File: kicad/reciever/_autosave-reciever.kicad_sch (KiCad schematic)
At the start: 12 parts, among them U2 LM2596T-5

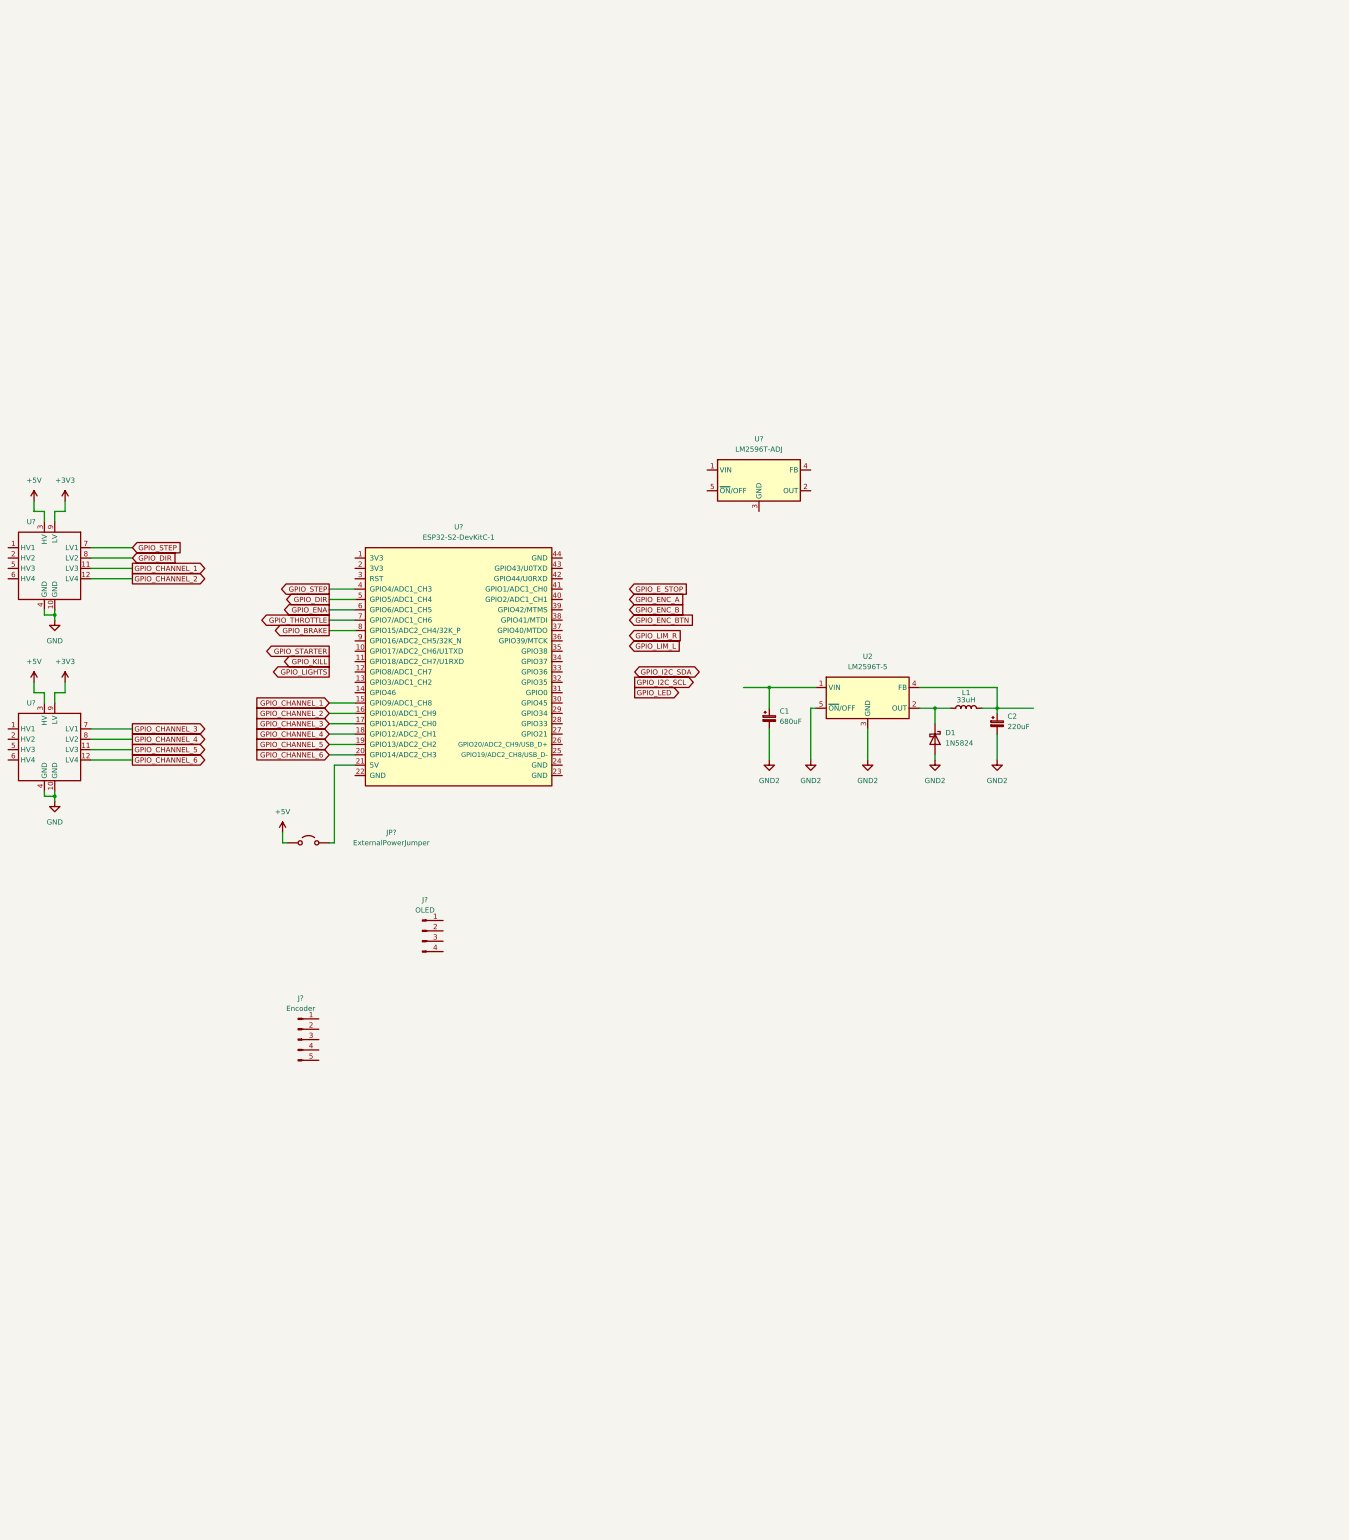
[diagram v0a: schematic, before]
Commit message: throttle servo behaves as expected, brake servo goes all the way and does not come back
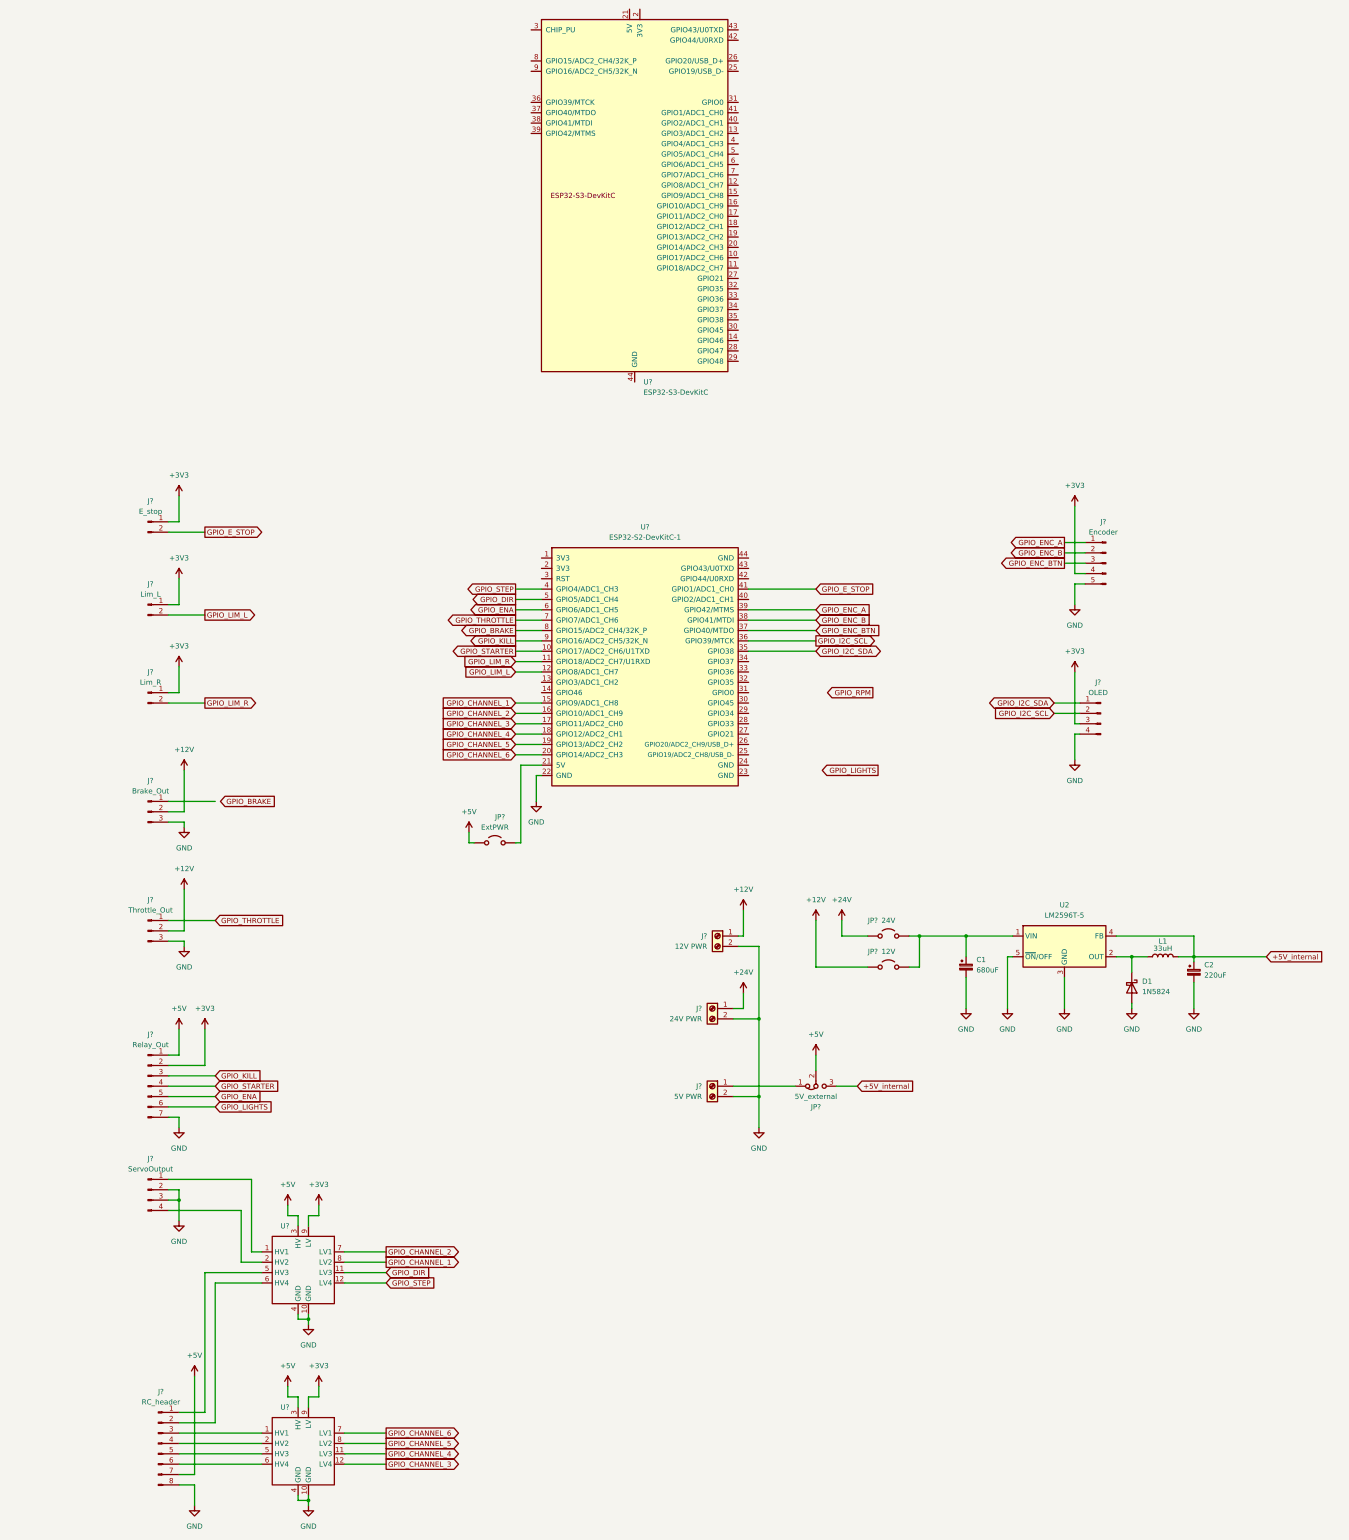
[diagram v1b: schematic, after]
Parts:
- removed U?: LM2596T-ADJ, Package_TO_SOT_THT:TO-220-5_P3.4x3.7mm_StaggerOdd_Lead3.8mm_Vertical, symbol Regulator_Switching:LM2596T-ADJ
- added J?: ServoOutput, symbol Connector:Conn_01x04_Pin
- added J?: 12V PWR, symbol Connector:Screw_Terminal_01x02
- added J?: Throttle_Out, symbol Connector:Conn_01x03_Pin
- added J?: Lim_L, symbol Connector:Conn_01x02_Pin
- added J?: 5V PWR, symbol Connector:Screw_Terminal_01x02
- added J?: Lim_R, symbol Connector:Conn_01x02_Pin
- added J?: Relay_Out, symbol Connector:Conn_01x07_Pin
- added J?: RC_header, symbol Connector:Conn_01x08_Pin
- added J?: Brake_Out, symbol Connector:Conn_01x03_Pin
- added J?: 24V PWR, symbol Connector:Screw_Terminal_01x02
- added J?: E_stop, symbol Connector:Conn_01x02_Pin
- added JP?: 5V_external, symbol Jumper:Jumper_3_Bridged12
- added JP?: 24V, symbol Jumper:Jumper_2_Open
- added JP?: 12V, symbol Jumper:Jumper_2_Open
- added U?: ESP32-S3-DevKitC, PCM_Espressif:ESP32-S3-DevKitC, symbol Espressif:ESP32-S3-DevKitC
- JP?: value ExternalPowerJumper -> ExtPWR
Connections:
- net GND2 is gone; now on net GND: C1.2, C2.2, D1.2 (A), U2.3 (GND), U2.5 (~{ON}/OFF)
- net +3V3: now also J?.3 (Pin_3), J?.4 (Pin_4), J?.1 (Pin_1), J?.1 (Pin_1), J?.1 (Pin_1), J?.2 (Pin_2)
- net +5V: now also J?.1 (Pin_1), J?.7 (Pin_7), JP?.2 (C)
- net GND: now also J?.4 (Pin_4), J?.5 (Pin_5), U?.22 (GND), J?.2 (Pin_2), J?.2 (Pin_2), J?.2 (Pin_2), J?.2 (Pin_2), J?.3 (Pin_3), J?.3 (Pin_3), J?.3 (Pin_3), J?.7 (Pin_7), J?.8 (Pin_8)
- net GPIO_CHANNEL_1: now also U?.8 (LV2); no longer U?.11 (LV3)
- net GPIO_CHANNEL_2: now also U?.7 (LV1); no longer U?.12 (LV4)
- net GPIO_CHANNEL_3: now also U?.12 (LV4); no longer U?.7 (LV1)
- net GPIO_CHANNEL_4: now also U?.11 (LV3); no longer U?.8 (LV2)
- net GPIO_CHANNEL_5: now also U?.8 (LV2); no longer U?.11 (LV3)
- net GPIO_CHANNEL_6: now also U?.7 (LV1); no longer U?.12 (LV4)
- net GPIO_DIR: now also U?.11 (LV3); no longer U?.8 (LV2)
- net GPIO_ENA: now also J?.5 (Pin_5)
- net GPIO_ENC_A: now also J?.1 (Pin_1), U?.39 (GPIO42/MTMS)
- net GPIO_ENC_B: now also J?.2 (Pin_2), U?.38 (GPIO41/MTDI)
- net GPIO_ENC_BTN: now also J?.3 (Pin_3), U?.37 (GPIO40/MTDO)
- net GPIO_E_STOP: now also U?.41 (GPIO1/ADC1_CH0), J?.2 (Pin_2)
- net GPIO_I2C_SCL: now also J?.2 (Pin_2), U?.36 (GPIO39/MTCK)
- net GPIO_I2C_SDA: now also J?.1 (Pin_1), U?.35 (GPIO38)
- net GPIO_KILL: now also U?.9 (GPIO16/ADC2_CH5/32K_N), J?.3 (Pin_3)
- net GPIO_LIGHTS: now also J?.6 (Pin_6)
- net GPIO_LIM_L: now also U?.12 (GPIO8/ADC1_CH7), J?.2 (Pin_2)
- net GPIO_LIM_R: now also U?.11 (GPIO18/ADC2_CH7/U1RXD), J?.2 (Pin_2)
- net GPIO_STARTER: now also U?.10 (GPIO17/ADC2_CH6/U1TXD), J?.4 (Pin_4)
- net GPIO_STEP: now also U?.12 (LV4); no longer U?.7 (LV1)
- net GPIO_THROTTLE: now also J?.1 (Pin_1)
- net at C1.1, U2.1 (VIN): now also JP?.2 (B), JP?.2 (B)
- net +5V_internal: now reaches C2.1, L1.2, U2.4 (FB)
- net +5V_internal: now also JP?.3 (B)
- net at U?.1 (HV1): now also J?.1 (Pin_1)
- net at U?.2 (HV2): now also J?.4 (Pin_4) (x2)
- net at U?.5 (HV3): now also J?.1 (Pin_1)
- net at U?.6 (HV4): now also J?.2 (Pin_2)
- net at U?.1 (HV1): now also J?.3 (Pin_3)
- net at U?.5 (HV3): now also J?.5 (Pin_5)
- net at U?.6 (HV4): now also J?.6 (Pin_6)
- new net: J?.1 (Pin_1), JP?.1 (A)
- new net: U?.1 (3V3), U?.2 (3V3)
- new net: U?.22 (GND), U?.23 (GND), U?.24 (GND), U?.44 (GND)
- new net +12V: J?.1 (Pin_1), J?.2 (Pin_2), J?.2 (Pin_2), JP?.1 (A)
- new net +24V: J?.1 (Pin_1), JP?.1 (A)
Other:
- moved on the sheet: C1, C2, D1, J?, JP?, L1, U2, U?
